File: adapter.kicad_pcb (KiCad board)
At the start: 2 copper layers, 100 x 80 mm, 11 parts, among them CN1 Molex_52602_0579, CN2 CONN_25X2, CN3 CONN_02X22

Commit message: Move CN1 footprint closer to PCB edge to improve fan clearance
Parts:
- moved CN1 10.0 mm to (178.0, 62.0)
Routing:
- net /D12: track 110.5 -> 123.6 mm
- net /D1: track 59.5 -> 72.5 mm
- net /D14: track 128.3 -> 140.9 mm
- net /D3: track 56.5 -> 68.9 mm
- net /xA13: track 31.4 -> 43.6 mm
- net GND2: track 25.9 -> 37.9 mm
- net /D0: track 61.6 -> 73.6 mm
- net /D15: track 137.1 -> 149.0 mm
- net /D10: track 86.3 -> 98.1 mm
- net /D13: track 118.3 -> 130.1 mm
- net /D5: track 53.1 -> 64.7 mm
- net /DMARQ: track 63.9 -> 75.4 mm
- net /xB13: track 38.0 -> 49.4 mm
- net /WRn: track 67.2 -> 78.5 mm
- net /D2: track 59.9 -> 71.2 mm
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
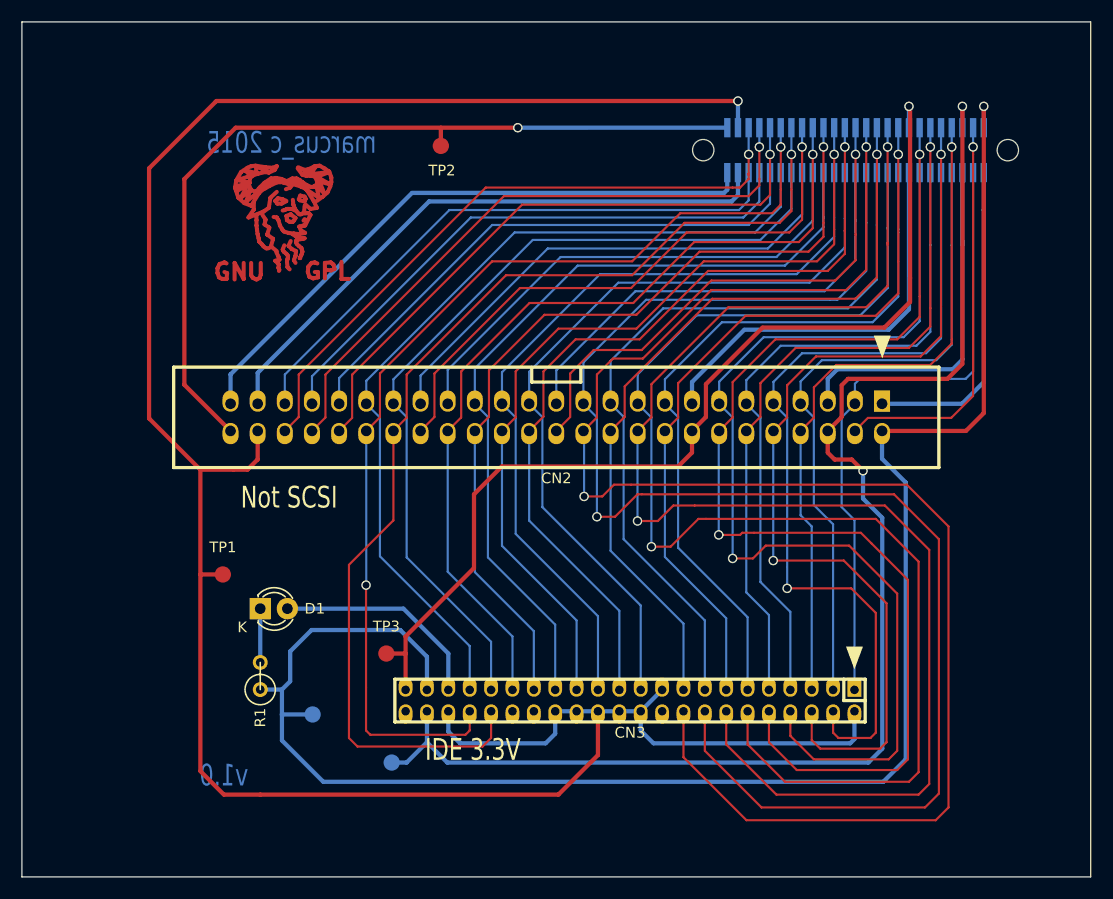
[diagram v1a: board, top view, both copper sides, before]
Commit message: Consolidate all power lines connected on the DC mainboard
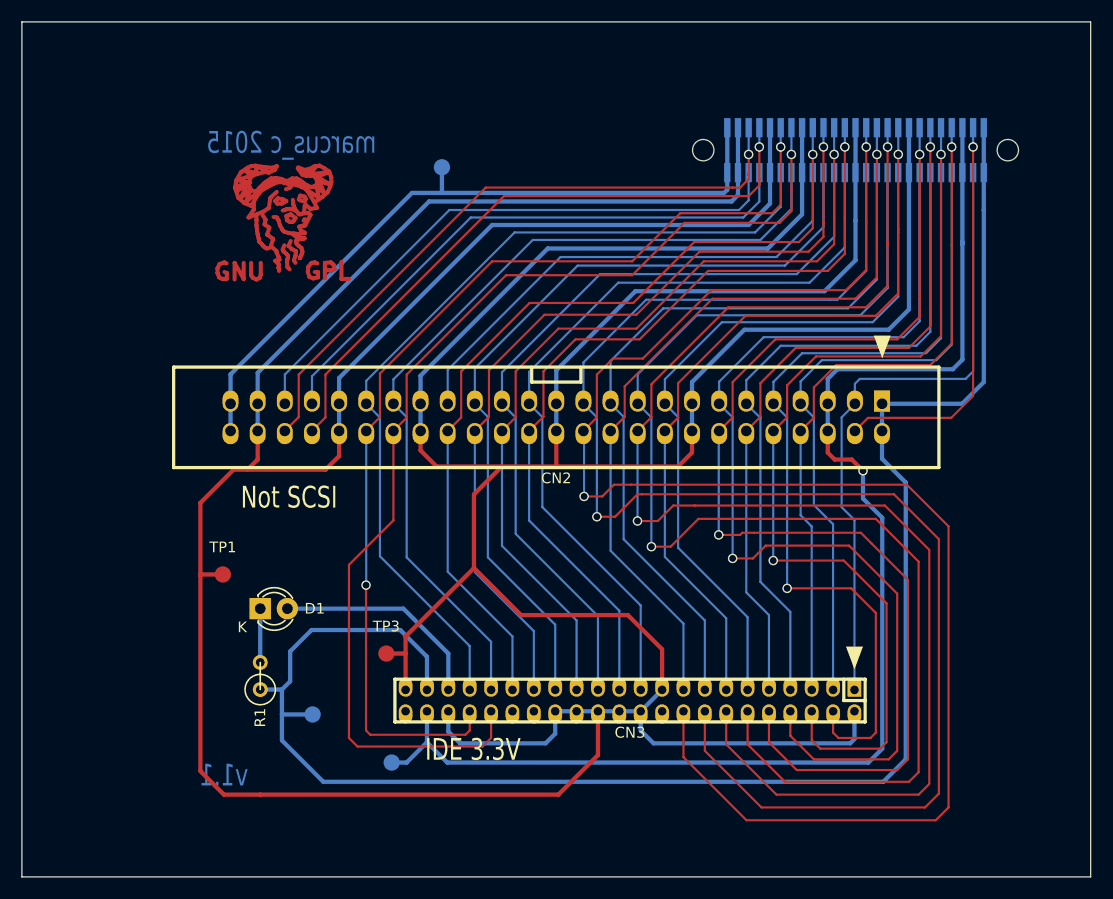
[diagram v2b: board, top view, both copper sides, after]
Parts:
- TP2: moved to B.Cu
- moved TP2 2.00 mm to (139.3, 63.6)
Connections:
- CN1 pad A1: +3V3_2 -> +3V3
- CN1 pad A13: /xA13 -> GND
- CN1 pad A18: /xA18 -> GND
- CN1 pad A21: /xA21 -> GND
- CN1 pad A24: P.GND_2 -> GND
- CN1 pad A25: +12V_2 -> +12V
- CN1 pad A3: +5V_2 -> +5V
- CN1 pad A8: GND2 -> GND
- CN1 pad B13: /xB13 -> GND
- CN1 pad B18: /xB18 -> GND
- CN1 pad B21: /xB21 -> GND
- CN1 pad B24: P.GND -> GND
- CN2 pad 1: +3V3_2 -> +3V3
- CN2 pad 15: GND2 -> GND
- CN2 pad 25: /xA13 -> GND
- CN2 pad 26: /xB13 -> GND
- CN2 pad 35: /xA18 -> GND
- CN2 pad 36: /xB18 -> GND
- CN2 pad 41: /xA21 -> GND
- CN2 pad 42: /xB21 -> GND
- CN2 pad 47: P.GND_2 -> GND
- CN2 pad 48: P.GND -> GND
- CN2 pad 49: +12V_2 -> +12V
- CN2 pad 5: +5V_2 -> +5V
- CN3 pad 19: P.GND -> GND
- CN3 pad 2: P.GND -> GND
- CN3 pad 22: P.GND -> GND
- CN3 pad 24: P.GND -> GND
- CN3 pad 26: P.GND -> GND
- CN3 pad 28: P.GND -> GND
- CN3 pad 30: P.GND -> GND
- CN3 pad 40: P.GND -> GND
- TP1 pad 1: P.GND -> GND
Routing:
- net GND: track 94.4 -> 500.6 mm, vias 1 -> 0
- net P.GND: track 223.6 -> 0.00 mm, vias 1 -> 0
- net /xB21: track 58.1 -> 0.00 mm, vias 1 -> 0
- net +12V_2: track 58.0 -> 0.00 mm
- net P.GND_2: track 56.8 -> 0.00 mm
- net /xB18: track 54.9 -> 0.00 mm, vias 1 -> 0
- net /xA21: track 52.4 -> 0.00 mm
- net /xB13: track 49.4 -> 0.00 mm, vias 1 -> 0
- net /xA18: track 48.5 -> 0.00 mm
- net /xA13: track 43.6 -> 0.00 mm
- net GND2: track 37.9 -> 0.00 mm
- net +5V_2: track 33.4 -> 0.00 mm
- net +3V3_2: track 30.0 -> 0.00 mm
- net +12V: track 79.9 -> 67.1 mm, vias 1 -> 0
- net +3V3: track 164.7 -> 160.5 mm, vias 1 -> 0
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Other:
- board text added: "v1.1"
- board text removed: "v1.0"
